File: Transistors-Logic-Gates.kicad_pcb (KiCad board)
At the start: 2 copper layers, 97.5 x 115.5 mm, 31 parts, among them J1 Conn_01x05_Socket, Q1 PN2222A, Q2 PN2222A, Q3 PN2222A, Q4 PN2222A, Q5 PN2222A, Q6 PN2222A, Q7 PN2222A, SW1 SW_SPDT, SW2 SW_SPDT, SW3 SW_SPDT, SW4 SW_SPDT, SW5 SW_Push, SW6 SW_SPDT, SW7 SW_SPDT

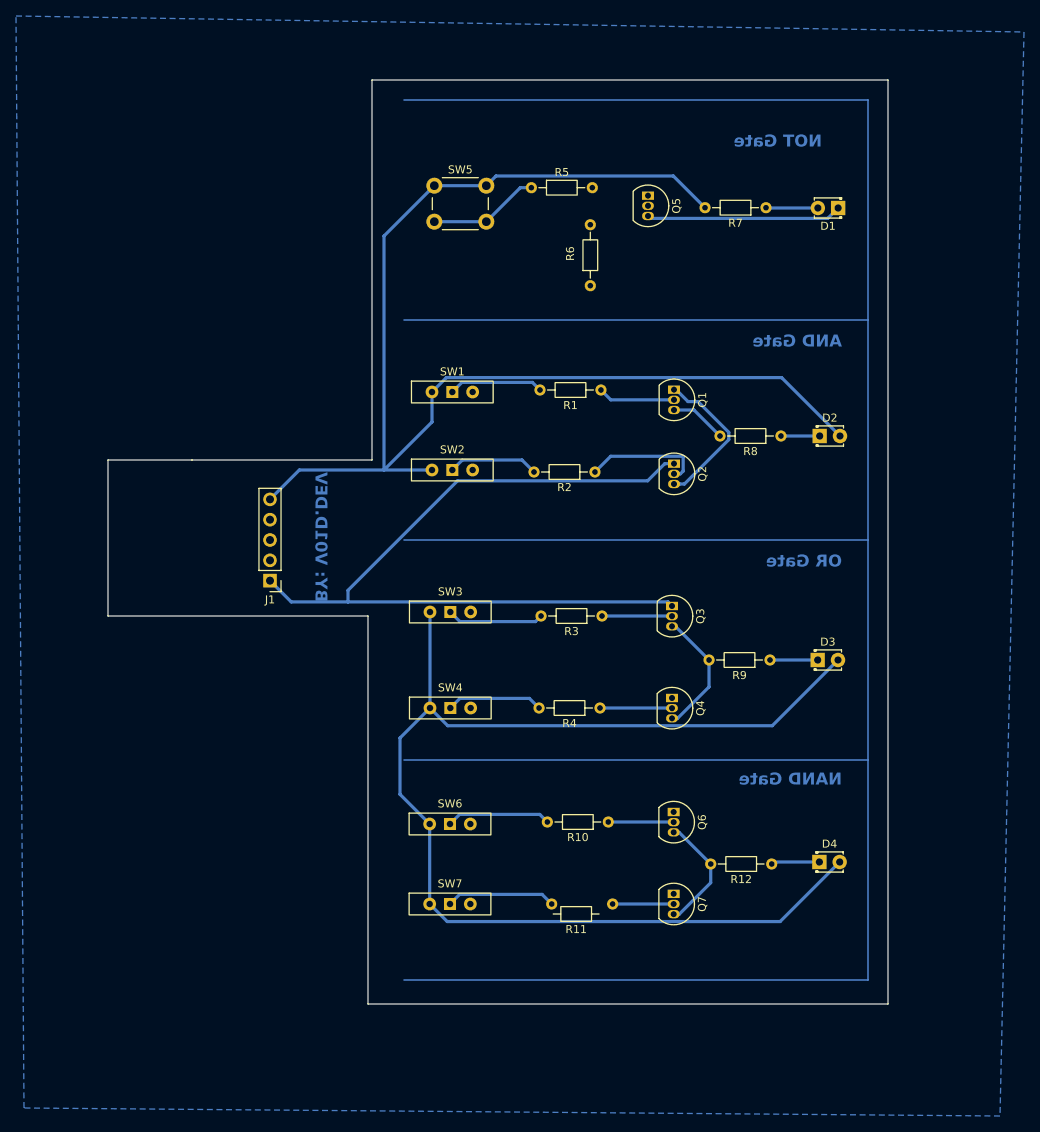
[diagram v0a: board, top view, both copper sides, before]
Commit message: feat: fixed GND plane, need to change minimums
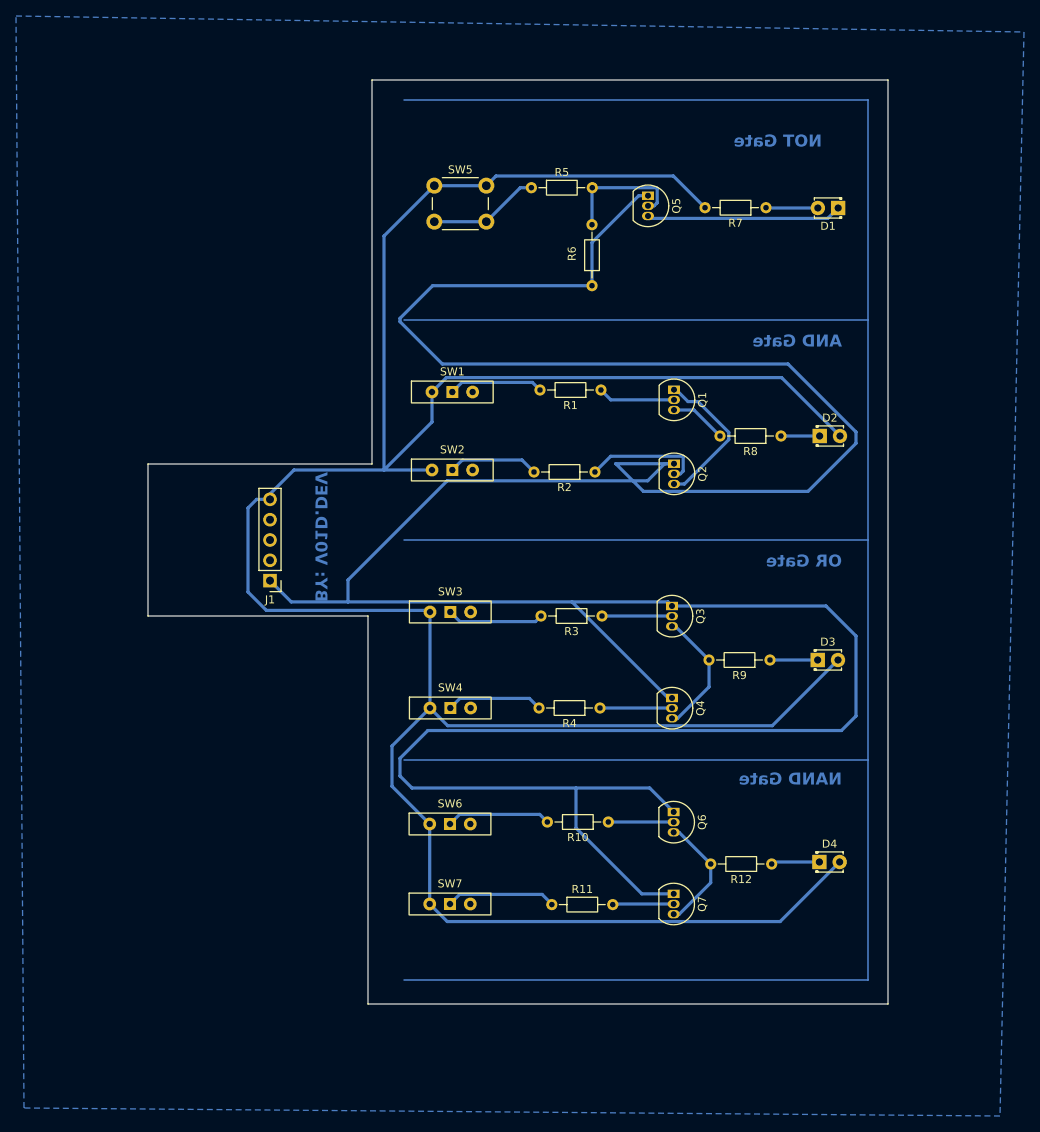
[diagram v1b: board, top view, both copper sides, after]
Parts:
- moved R11 6.95 mm to (140.5, 135.6), turned to 0 degrees
- moved R6 0.21 mm to (145.5, 58.2)
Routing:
- net /GND: track 100.3 -> 417.5 mm
- net /Vcc: track 313.1 -> 351.8 mm
- net Net-(Q5-B): track 0.00 -> 15.9 mm
- net Net-(Q1-E): track 19.8 -> 18.9 mm
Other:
- board size 97.5 x 115.5 mm -> 92.5 x 115.5 mm
